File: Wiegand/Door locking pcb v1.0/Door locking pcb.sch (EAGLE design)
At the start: 52 parts, among them CON1 SPI, J1 22--02, J7 22--02, Q3 BSP75, X3 16MHz, X4 MINI-USB

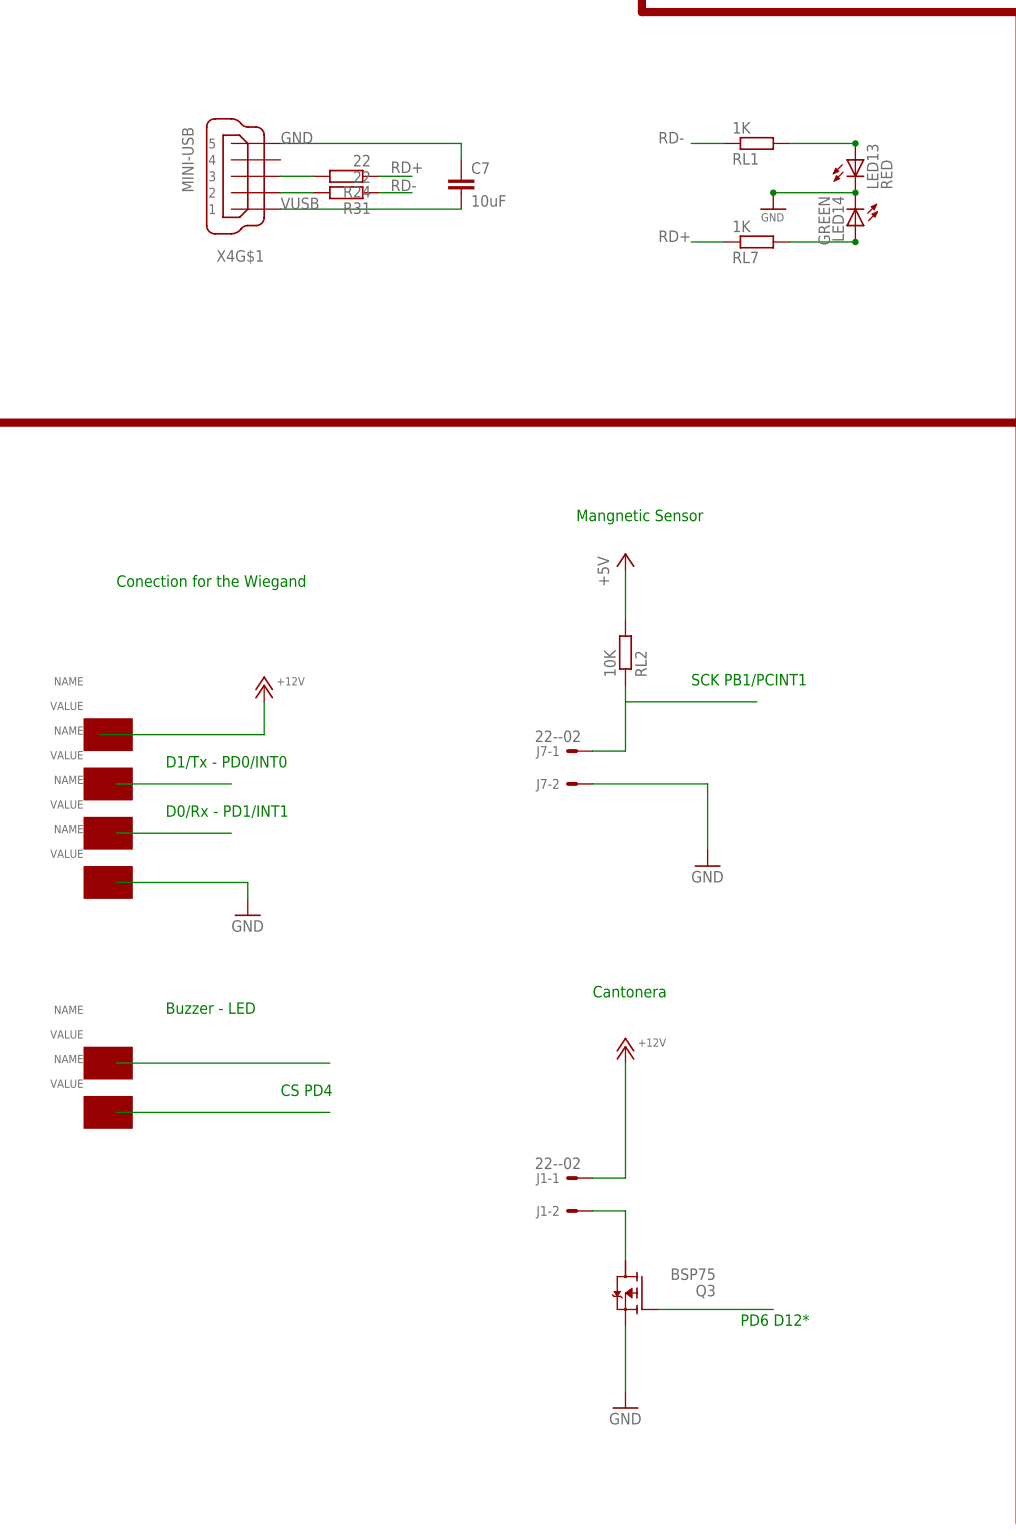
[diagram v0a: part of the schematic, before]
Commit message: corrected errors in wiedgand
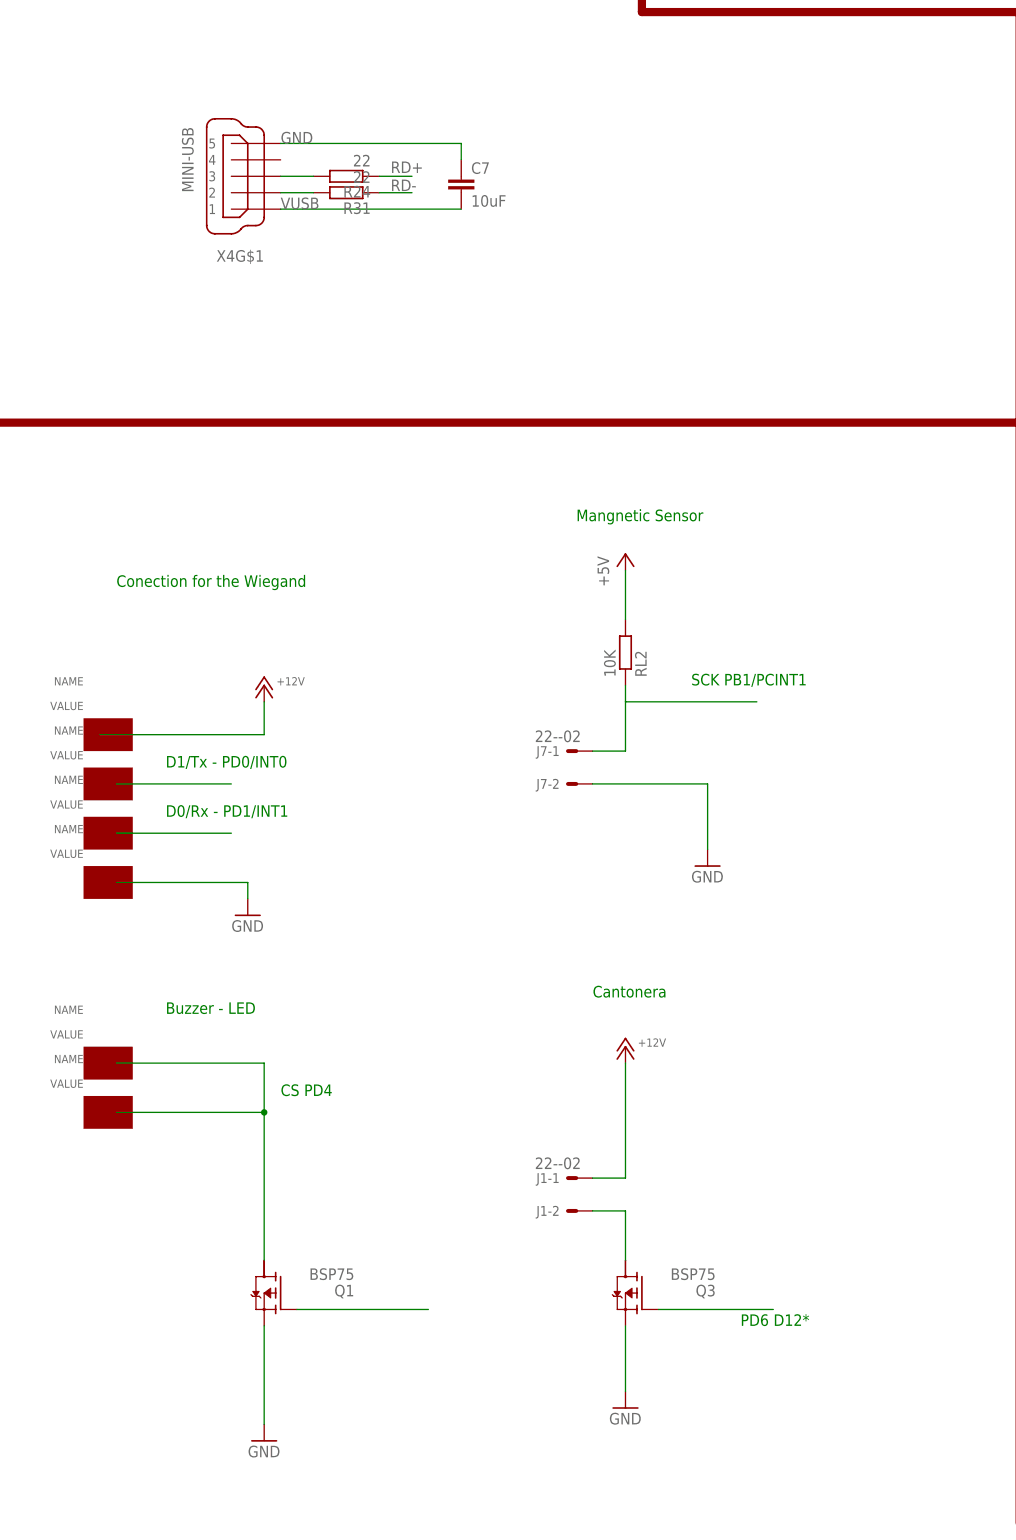
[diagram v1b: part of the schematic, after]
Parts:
- removed LED13: RED, adafruit:LEDCHIPLED_1206
- removed LED14: GREEN, adafruit:LEDCHIPLED_1206
- removed RL1, RL7: 1K, rcl:R-EU_R0805
- added Q1: BSP75, infineon:BSP613P
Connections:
- removed net N$14: LED14.A, RL7.2
- removed net N$8: LED13.A, RL1.2
- new net N$1: PIN3.1, PIN4.1, Q1.D@1
- net CS: now also Q1.G; no longer PIN3.1, PIN4.1
- net GND: now also Q1.S; no longer LED13.C, LED14.C
- net RD+: no longer RL7.1
- net RD-: no longer RL1.1
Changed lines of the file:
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@@
 <?xml version="1.0" encoding="utf-8"?>
 <!DOCTYPE eagle SYSTEM "eagle.dtd">
-<eagle version="6.6.0">
+<eagle version="7.0.0">
 <drawing>
 <settings>
@@
 <part name="C12" library="rcl" deviceset="C-EU" device="C1206" value="100nF"/>
 <part name="D4" library="lpatiny" deviceset="1N581*" device="D1206" value="1N581D1206"/>
-<part name="RL1" library="rcl" deviceset="R-EU_" device="R0805" value="1K"/>
-<part name="RL7" library="rcl" deviceset="R-EU_" device="R0805" value="1K"/>
-<part name="GND1" library="supply1" deviceset="GND" device=""/>
 <part name="U$4" library="adafruit" deviceset="ATMEGA32U4" device="-AU"/>
 <part name="GND28" library="supply1" deviceset="GND" device=""/>
@@
 <part name="GND39" library="supply1" deviceset="GND" device=""/>
 <part name="J7" library="lpatiny" deviceset="22-?-02" device="" value="22--02"/>
-<part name="LED13" library="adafruit" deviceset="LED" device="CHIPLED_1206" value="RED"/>
-<part name="LED14" library="adafruit" deviceset="LED" device="CHIPLED_1206" value="GREEN"/>
 <part name="GND5" library="supply1" deviceset="GND" device=""/>
 <part name="RL5" library="rcl" deviceset="R-EU_" device="R0805" value="1K"/>
@@
 <part name="GND3" library="supply1" deviceset="GND" device=""/>
 <part name="Q3" library="infineon" deviceset="BSP613P" device="" value="BSP75"/>
+<part name="Q1" library="infineon" deviceset="BSP613P" device="" value="BSP75"/>
+<part name="GND6" library="supply1" deviceset="GND" device=""/>
 </parts>
 <sheets>
@@
 <instance part="C12" gate="G$1" x="284.48" y="144.78" rot="MR180"/>
 <instance part="D4" gate="G$1" x="248.92" y="142.24"/>
-<instance part="RL1" gate="G$1" x="45.72" y="165.1" rot="MR180"/>
-<instance part="RL7" gate="G$1" x="45.72" y="149.86" rot="MR180"/>
-<instance part="GND1" gate="1" x="48.26" y="154.94" smashed="yes">
-<attribute name="VALUE" x="46.355" y="153.035" size="1.27" layer="96"/>
-</instance>
 <instance part="U$4" gate="G$1" x="220.98" y="45.72"/>
 <instance part="GND28" gate="1" x="144.78" y="73.66"/>
@@
 <instance part="J7" gate="-1" x="17.78" y="71.12" rot="MR0"/>
 <instance part="J7" gate="-2" x="17.78" y="66.04" rot="MR0"/>
-<instance part="LED13" gate="G$1" x="60.96" y="162.56"/>
-<instance part="LED14" gate="G$1" x="60.96" y="152.4" rot="R180"/>
 <instance part="GND5" gate="1" x="-33.02" y="45.72"/>
 <instance part="RL5" gate="G$1" x="-5.08" y="254" rot="MR180"/>
@@
 <instance part="GND3" gate="1" x="25.4" y="-30.48"/>
 <instance part="Q3" gate="G$1" x="27.94" y="-12.7" rot="MR0"/>
+<instance part="Q1" gate="G$1" x="-27.94" y="-12.7" rot="MR0"/>
+<instance part="GND6" gate="1" x="-30.48" y="-35.56"/>
 </instances>
 <busses>
@@
 <wire x1="284.48" y1="142.24" x2="276.86" y2="142.24" width="0.1524" layer="91"/>
 <junction x="284.48" y="142.24"/>
-</segment>
-<segment>
-<wire x1="60.96" y1="157.48" x2="48.26" y2="157.48" width="0.1524" layer="91"/>
-<pinref part="GND1" gate="1" pin="GND"/>
-<pinref part="LED13" gate="G$1" pin="C"/>
-<pinref part="LED14" gate="G$1" pin="C"/>
-<junction x="60.96" y="157.48"/>
-<junction x="48.26" y="157.48"/>
 </segment>
 <segment>
@@
 <pinref part="Q3" gate="G$1" pin="S"/>
 </segment>
+<segment>
+<pinref part="GND6" gate="1" pin="GND"/>
+<wire x1="-30.48" y1="-33.02" x2="-30.48" y2="-17.78" width="0.1524" layer="91"/>
+<pinref part="Q1" gate="G$1" pin="S"/>
+</segment>
 </net>
 <net name="SCK" class="0">
@@
 <net name="RD-" class="0">
 <segment>
-<pinref part="RL1" gate="G$1" pin="1"/>
-<wire x1="40.64" y1="165.1" x2="35.56" y2="165.1" width="0.1524" layer="91"/>
-<label x="30.48" y="165.1" size="1.778" layer="95"/>
-</segment>
-<segment>
 <pinref part="U$4" gate="G$1" pin="D-"/>
 <wire x1="198.12" y1="60.96" x2="180.34" y2="60.96" width="0.1524" layer="91"/>
@@
 </net>
 <net name="RD+" class="0">
-<segment>
-<pinref part="RL7" gate="G$1" pin="1"/>
-<wire x1="40.64" y1="149.86" x2="35.56" y2="149.86" width="0.1524" layer="91"/>
-<label x="30.48" y="149.86" size="1.778" layer="95"/>
-</segment>
 <segment>
 <pinref part="U$4" gate="G$1" pin="D+"/>
@@
 </segment>
 <segment>
-<wire x1="-53.34" y1="22.86" x2="-20.32" y2="22.86" width="0.1524" layer="91"/>
-<pinref part="PIN3" gate="G$1" pin="1"/>
-</segment>
-<segment>
-<wire x1="-53.34" y1="15.24" x2="-20.32" y2="15.24" width="0.1524" layer="91"/>
-<pinref part="PIN4" gate="G$1" pin="1"/>
+<pinref part="Q1" gate="G$1" pin="G"/>
+<wire x1="-5.08" y1="-15.24" x2="-25.4" y2="-15.24" width="0.1524" layer="91"/>
 </segment>
 </net>
@@
 <wire x1="-27.94" y1="160.02" x2="-22.86" y2="160.02" width="0.1524" layer="91"/>
 <pinref part="R24" gate="G$1" pin="2"/>
-</segment>
-</net>
-<net name="N$8" class="0">
-<segment>
-<pinref part="RL1" gate="G$1" pin="2"/>
-<wire x1="50.8" y1="165.1" x2="60.96" y2="165.1" width="0.1524" layer="91"/>
-<pinref part="LED13" gate="G$1" pin="A"/>
-<junction x="60.96" y="165.1"/>
-</segment>
-</net>
-<net name="N$14" class="0">
-<segment>
-<pinref part="RL7" gate="G$1" pin="2"/>
-<wire x1="60.96" y1="149.86" x2="50.8" y2="149.86" width="0.1524" layer="91"/>
-<pinref part="LED14" gate="G$1" pin="A"/>
-<junction x="60.96" y="149.86"/>
 </segment>
 </net>
@@
 </segment>
 </net>
+<net name="N$1" class="0">
+<segment>
+<pinref part="Q1" gate="G$1" pin="D@1"/>
+<wire x1="-30.48" y1="-7.62" x2="-30.48" y2="15.24" width="0.1524" layer="91"/>
+<pinref part="PIN4" gate="G$1" pin="1"/>
+<wire x1="-30.48" y1="15.24" x2="-53.34" y2="15.24" width="0.1524" layer="91"/>
+<wire x1="-30.48" y1="15.24" x2="-30.48" y2="22.86" width="0.1524" layer="91"/>
+<pinref part="PIN3" gate="G$1" pin="1"/>
+<wire x1="-30.48" y1="22.86" x2="-53.34" y2="22.86" width="0.1524" layer="91"/>
+<junction x="-30.48" y="15.24"/>
+</segment>
+</net>
